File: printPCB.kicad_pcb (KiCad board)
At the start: 2 copper layers, 68.6 x 53.3 mm, 14 parts, among them P1 Power, P2 Analog, P3 Digital, P4 Digital, P5 CONN_01X01, P6 CONN_01X01, P7 CONN_01X01, P8 CONN_01X01

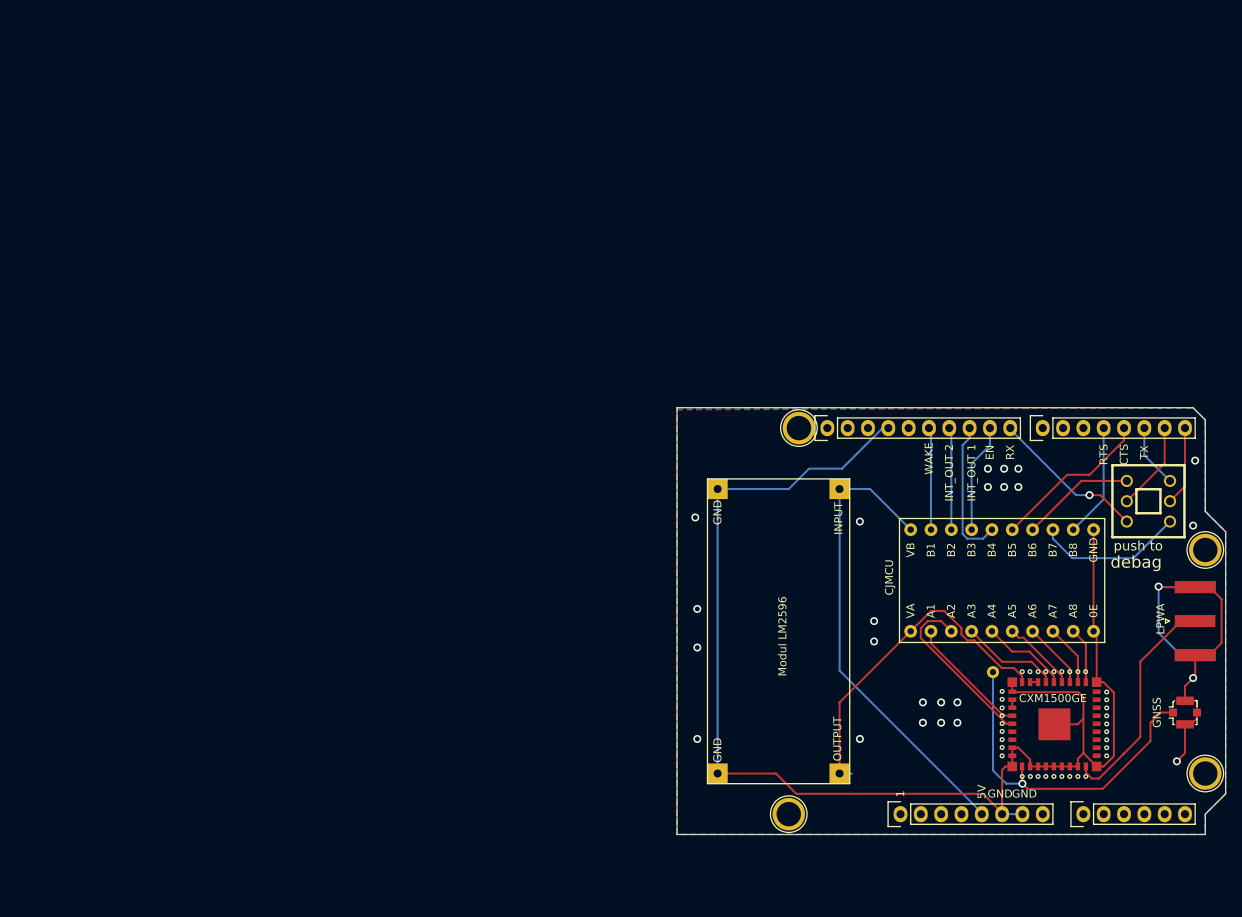
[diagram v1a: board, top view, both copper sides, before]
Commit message: mengubah routing pada jalur sinyal rf agar impedasi 50 ohm dan menambah file duplicate print pcb
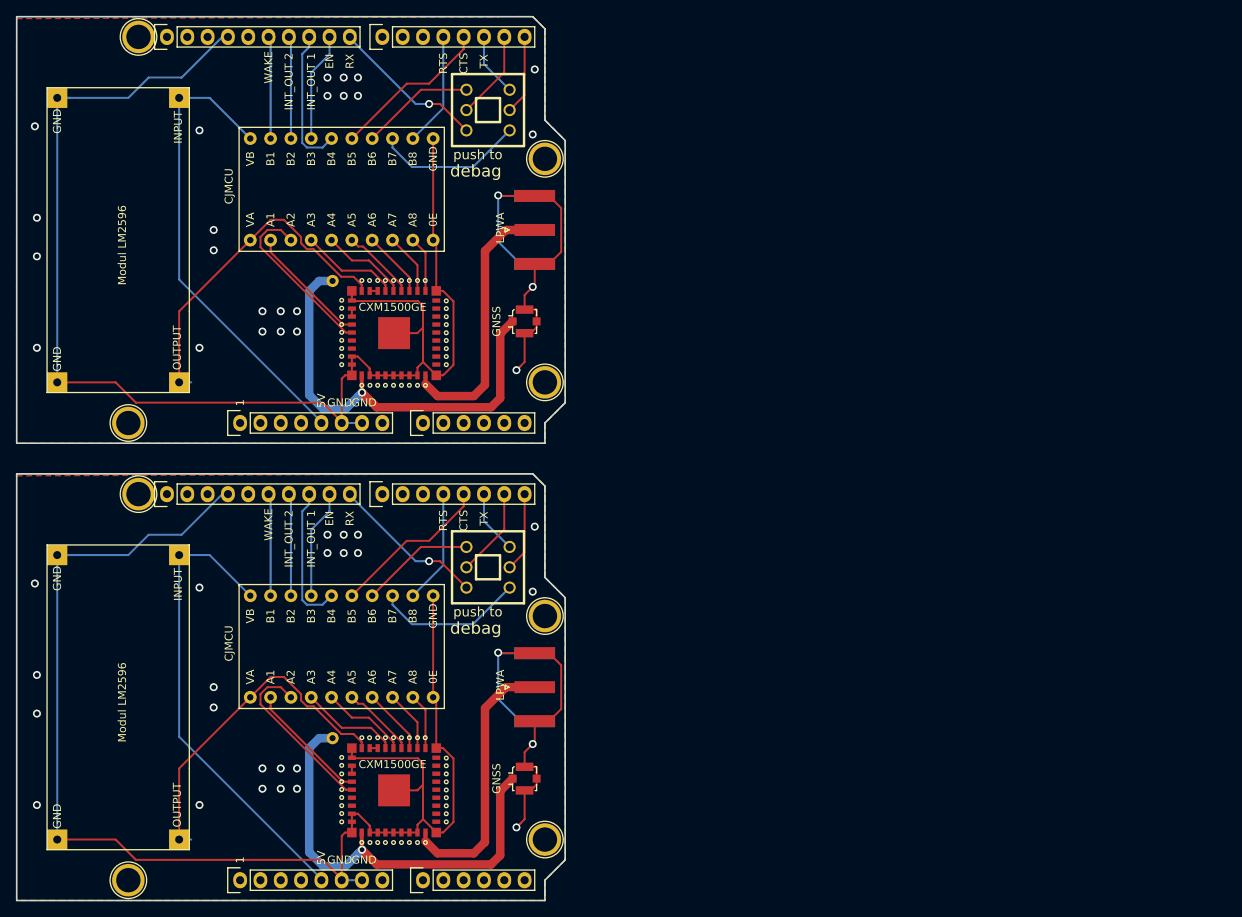
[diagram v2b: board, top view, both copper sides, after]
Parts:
- added CJMCU: modul_lvl-conveter_cjmcu, modul:modul_lvl_conveter_cjmcu, F.Cu at (57.7, 109.2)
- added CXM1500GE: CXM1500GE, modul:CXM1500GE, F.Cu at (70.4, 115.6)
- added GNSS: SMA, Connector_Coaxial:U.FL_Molex_MCRF_73412-0110_Vertical, F.Cu at (91.9, 119.4)
- added LM2596_1: modul_dc-dc_lm2596, modul:modul_lvl_dc-dc_lm2596, F.Cu at (42.4, 95.2)
- added LPWA: SMA, Connector_Coaxial:SMA_Amphenol_132289_EdgeMount, F.Cu at (93.2, 108.0)
- added P1: Power, Socket_Arduino_Uno:Socket_Strip_Arduino_1x08, F.Cu at (56.4, 132.1)
- added P2: Analog, Socket_Arduino_Uno:Socket_Strip_Arduino_1x06, F.Cu at (79.2, 132.1)
- added P3: Digital, Socket_Arduino_Uno:Socket_Strip_Arduino_1x10, F.Cu at (47.2, 83.8)
- added P4: Digital, Socket_Arduino_Uno:Socket_Strip_Arduino_1x08, F.Cu at (74.2, 83.8)
- added P5: CONN_01X01, Socket_Arduino_Uno:Arduino_1pin, F.Cu at (42.4, 132.1)
- added P6: CONN_01X01, Socket_Arduino_Uno:Arduino_1pin, F.Cu at (94.5, 127.0)
- added P7: CONN_01X01, Socket_Arduino_Uno:Arduino_1pin, F.Cu at (43.7, 83.8)
- added P8: CONN_01X01, Socket_Arduino_Uno:Arduino_1pin, F.Cu at (94.5, 99.1)
- added push to: SWITCH-DPDT, Switches:Switch_DPDT_6p_TH, F.Cu at (87.4, 93.0)
- moved LM2596_1 95.9 mm to (42.4, 38.1)
- moved P6 95.9 mm to (94.5, 69.8)
- moved P8 95.9 mm to (94.5, 41.9)
- moved CJMCU 95.9 mm to (57.7, 52.1)
- moved GNSS 95.9 mm to (91.9, 62.2)
- moved LPWA 95.9 mm to (93.2, 50.8)
- moved P2 95.9 mm to (79.2, 74.9)
- moved P3 95.9 mm to (47.2, 26.7)
- moved P5 95.9 mm to (42.4, 74.9)
- moved P7 95.9 mm to (43.7, 26.7)
- moved CXM1500GE 95.9 mm to (70.4, 58.4)
- moved P1 95.9 mm to (56.4, 74.9)
- moved P4 95.9 mm to (74.2, 26.7)
- moved push to 95.9 mm to (87.4, 35.8)
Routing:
- net (no net): track 0.00 -> 690.6 mm, vias 0 -> 27
- net Net-(J1-Pad1): track 43.3 -> 55.6 mm
- net Net-(J2-Pad1): track 28.6 -> 33.8 mm
- added copper zone on B.Cu, net (none)
- added copper zone on F.Cu, net (none)
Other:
- board size 68.6 x 53.3 mm -> 68.6 x 110.5 mm
- net class rf added: clearance 0.2, trace_width 1.05736, via_dia 0.6, via_drill 0.4
